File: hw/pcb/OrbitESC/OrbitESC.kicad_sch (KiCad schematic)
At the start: 0 parts

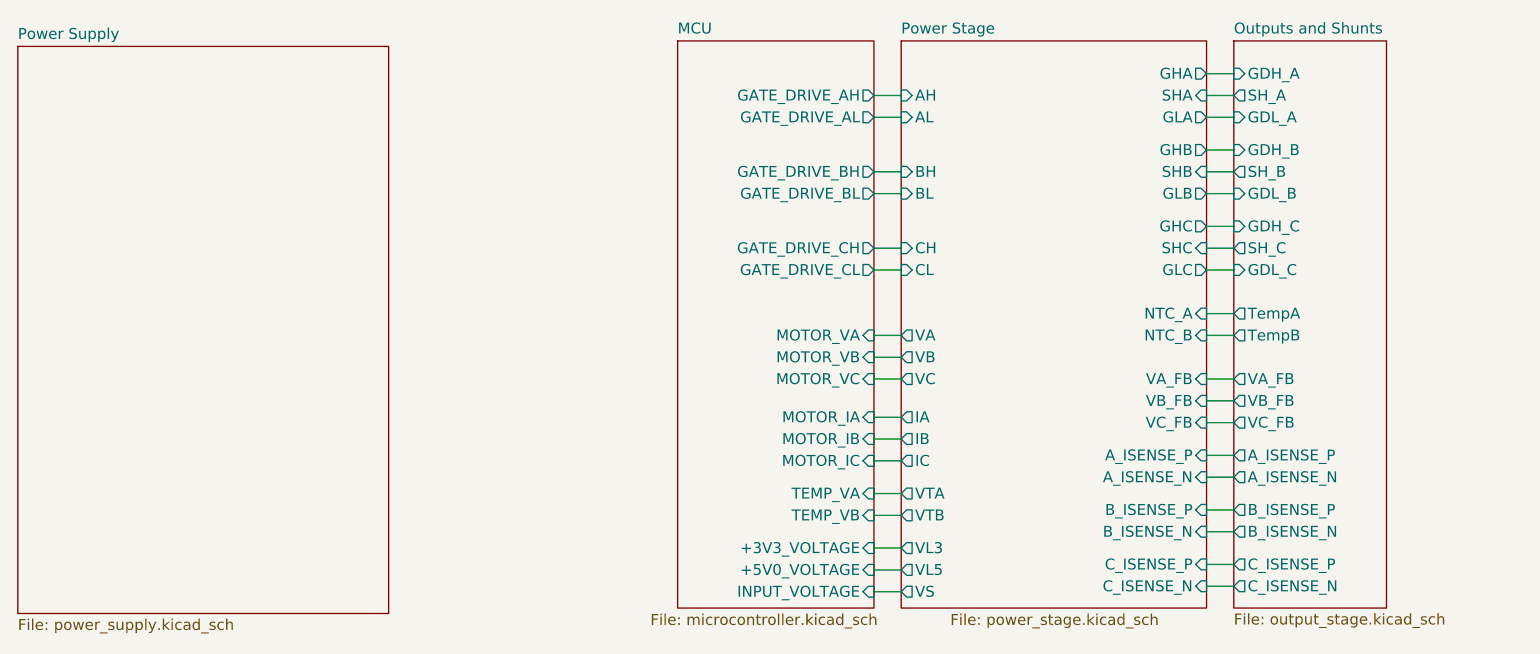
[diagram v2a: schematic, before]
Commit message: Start rework of processor selection after realizing I can't afford manufacturing...
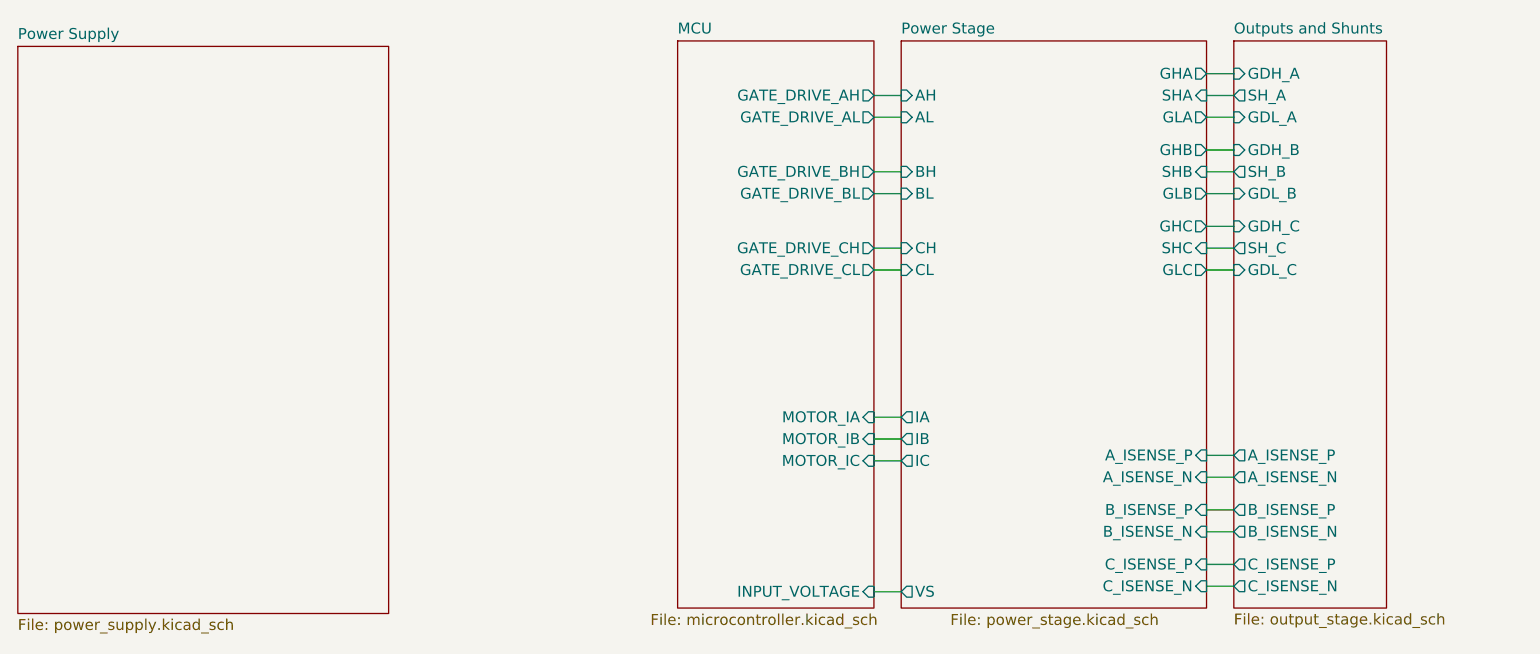
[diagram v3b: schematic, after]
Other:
- sheet MCU ports: added none; removed +3V3_VOLTAGE, +5V0_VOLTAGE, MOTOR_VA, MOTOR_VB, MOTOR_VC, TEMP_VA, TEMP_VB
- sheet Outputs and Shunts ports: added none; removed TempA, TempB, VA_FB, VB_FB, VC_FB
- sheet Power Stage ports: added none; removed NTC_A, NTC_B, VA, VA_FB, VB, VB_FB, VC, VC_FB, VL3, VL5, VTA, VTB
